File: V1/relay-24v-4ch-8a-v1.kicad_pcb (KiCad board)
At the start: 2 copper layers, 53 x 67.8 mm, 24 parts, among them J1 DB141V-2.54-2P, J2 DB141V-2.54-4P, J3 DB142V-5.08-4P, J4 DB142V-5.08-4P, K1 G5Q-1A4-DC24V, K2 G5Q-1A4-DC24V, K3 G5Q-1A4-DC24V, K4 G5Q-1A4-DC24V

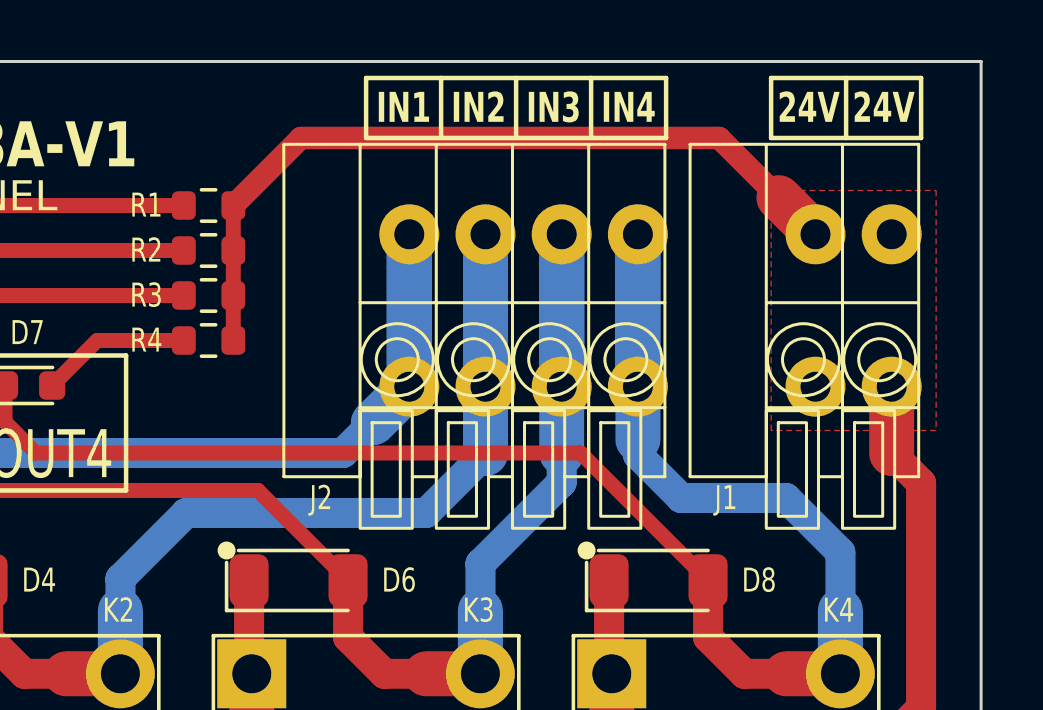
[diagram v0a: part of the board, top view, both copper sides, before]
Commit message: Replaced terminal blocks
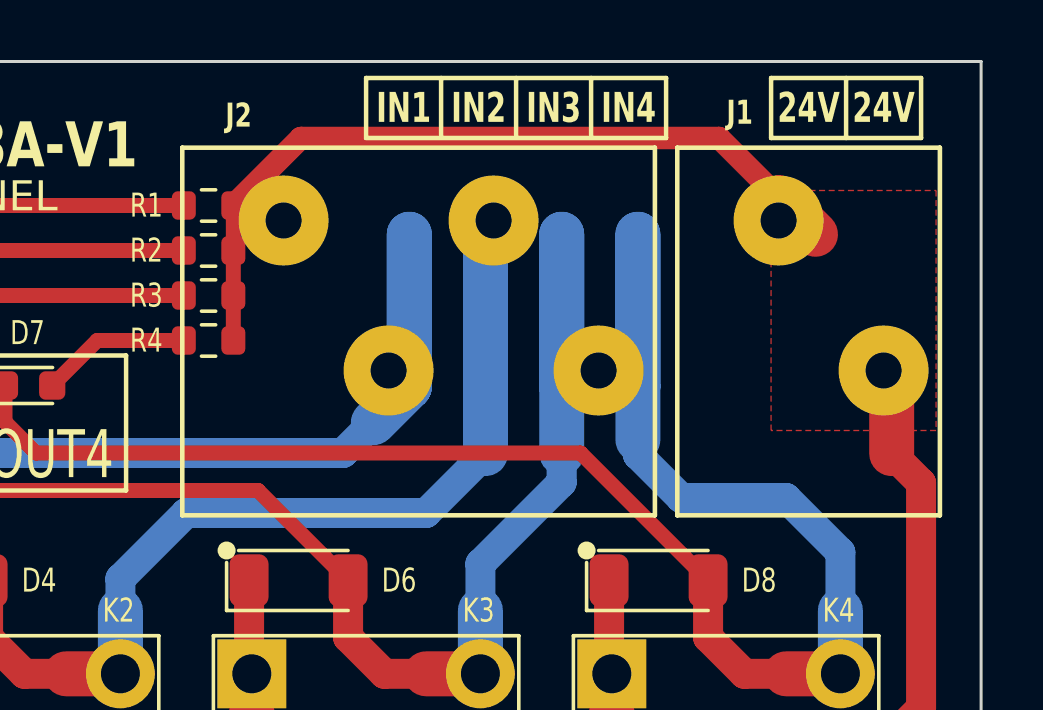
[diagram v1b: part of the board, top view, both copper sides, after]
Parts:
- J1: value DB141V-2.54-2P -> 250-202; footprint Tales:TerminalBlock_Dibo_DB141V-2.54-2P_1x02_P2.54mm_Vertical -> Tales:TerminalBlock_Wago_250-202_1x02_P3.5mm_45Degree
- J2: value DB141V-2.54-4P -> 250-204; footprint Tales:TerminalBlock_Dibo_DB141V-2.54-4P_1x04_P2.54mm_Vertical -> Tales:TerminalBlock_Wago_250-204_1x04_P3.5mm_45Degree
- moved J2 2.80 mm to (160.0, 70.0), turned to 0 degrees
- moved J1 0.90 mm to (173.0, 70.0), turned to 0 degrees
